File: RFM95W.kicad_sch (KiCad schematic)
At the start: 2 parts, among them U2 RFM95W-915S2

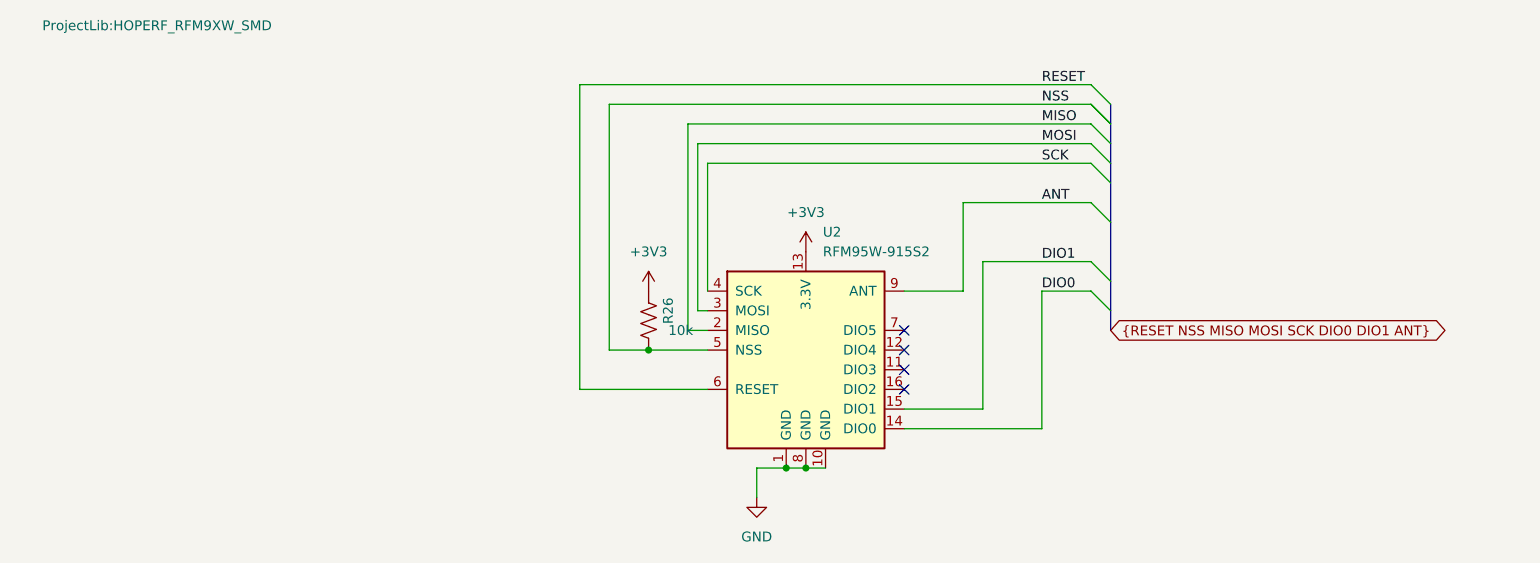
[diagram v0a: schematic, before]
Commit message: ongoing conversion to put f411 on board rather than pinsocket.
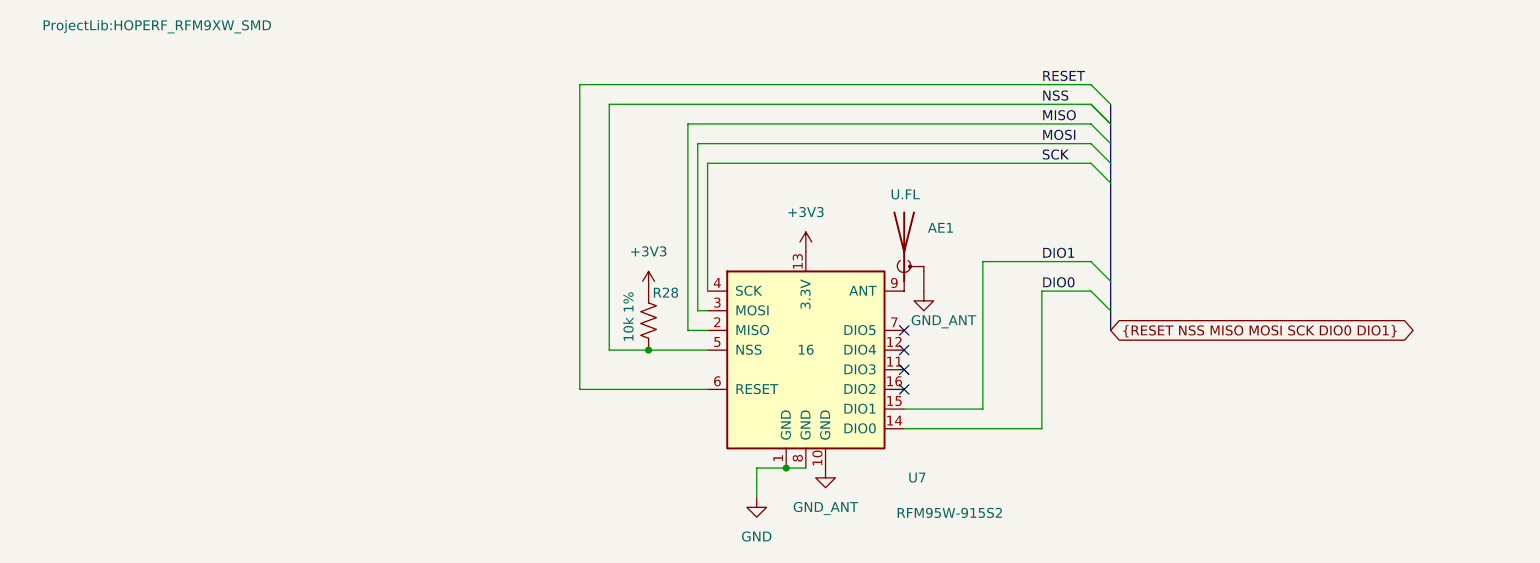
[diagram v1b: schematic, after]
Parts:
- removed R26: 10k, ProjectLib:R_0603_1608Metric, symbol ProjectLib:R_US
- added AE1: U.FL, ProjectLib:U.FL_Molex_MCRF_73412-0110_Vertical, symbol ProjectLib:Antenna_Shield
- added R28: 10k 1%, ProjectLib:R_0402_1005Metric, symbol ProjectLib:R_US
- U7: renamed from U2; Package (none) -> HOPERF_RFM9XW_SMD; pads (none) -> 16
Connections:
- net +3V3: now also R28.1
- net GND: no longer U7.10 (GND)
- net NSS: now also R28.2
- net ANT: no longer names the net of U7.9 (ANT)
- net ANT: now also AE1.1 (A)
- new net GND_ANT: AE1.2 (Shield), U7.10 (GND)
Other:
- title: Multiplex I2C to Screw Terminal connectors -> ADCs for 10K thermistors

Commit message: ongoing add of MCU, etc.
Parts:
- renumbered AE1 to AE?, R28 to R?, U7 to U?
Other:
- title: ADCs for 10K thermistors -> Multiplex I2C to Screw Terminal connectors
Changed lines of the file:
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@@
 	(paper "A4")
 	(title_block
-		(title "ADCs for 10K thermistors")
-		(date "2025-01-07")
-		(rev "v0.1.1")
+		(title "Multiplex I2C to Screw Terminal connectors")
+		(date "2025-09-07")
+		(rev "v0.2.0")
 	)
 	(bus_alias "SPI"
@@
 		(on_board yes)
 		(dnp no)
-		(property "Reference" "R28"
+		(property "Reference" "R?"
 			(at 95.758 77.724 0)
 			(effects
@@
 		)
 		(instances
-			(project ""
-				(path "/0c2d0c14-8850-4a30-bb78-b2f40cb442ba/2db29b35-1005-45eb-b852-0b853354466f"
-					(reference "R28")
+			(project "multiplexI2C"
+				(path "/0c2d0c14-8850-4a30-bb78-b2f40cb442ba/8bb5a1a1-4d5b-4032-b28f-cb44ec0cd683"
+					(reference "R?")
 					(unit 1)
 				)
@@
 		(dnp no)
 		(fields_autoplaced yes)
-		(property "Reference" "#PWR066"
+		(property "Reference" "#PWR0104"
 			(at 118.11 106.68 0)
 			(effects
@@
 		)
 		(instances
-			(project ""
-				(path "/0c2d0c14-8850-4a30-bb78-b2f40cb442ba/2db29b35-1005-45eb-b852-0b853354466f"
-					(reference "#PWR066")
+			(project "multiplexI2C"
+				(path "/0c2d0c14-8850-4a30-bb78-b2f40cb442ba/8bb5a1a1-4d5b-4032-b28f-cb44ec0cd683"
+					(reference "#PWR0104")
 					(unit 1)
 				)
@@
 		(on_board yes)
 		(dnp no)
-		(property "Reference" "#PWR065"
+		(property "Reference" "#PWR0105"
 			(at 130.81 83.82 0)
 			(effects
@@
 		)
 		(instances
-			(project ""
-				(path "/0c2d0c14-8850-4a30-bb78-b2f40cb442ba/2db29b35-1005-45eb-b852-0b853354466f"
-					(reference "#PWR065")
+			(project "multiplexI2C"
+				(path "/0c2d0c14-8850-4a30-bb78-b2f40cb442ba/8bb5a1a1-4d5b-4032-b28f-cb44ec0cd683"
+					(reference "#PWR0105")
 					(unit 1)
 				)
@@
 		)
 		(instances
-			(project "SensorProject_t16-pcb"
-				(path "/0c2d0c14-8850-4a30-bb78-b2f40cb442ba/2db29b35-1005-45eb-b852-0b853354466f"
+			(project "multiplexI2C"
+				(path "/0c2d0c14-8850-4a30-bb78-b2f40cb442ba/8bb5a1a1-4d5b-4032-b28f-cb44ec0cd683"
 					(reference "#PWR0102")
 					(unit 1)
@@
 		(dnp no)
 		(fields_autoplaced yes)
-		(property "Reference" "#PWR0103"
+		(property "Reference" "#PWR0101"
 			(at 109.22 110.49 0)
 			(effects
@@
 		)
 		(instances
-			(project "SensorProject_t16-pcb"
-				(path "/0c2d0c14-8850-4a30-bb78-b2f40cb442ba/2db29b35-1005-45eb-b852-0b853354466f"
-					(reference "#PWR0103")
+			(project "multiplexI2C"
+				(path "/0c2d0c14-8850-4a30-bb78-b2f40cb442ba/8bb5a1a1-4d5b-4032-b28f-cb44ec0cd683"
+					(reference "#PWR0101")
 					(unit 1)
 				)
@@
 		(dnp no)
 		(fields_autoplaced yes)
-		(property "Reference" "#PWR0101"
+		(property "Reference" "#PWR0103"
 			(at 115.57 76.2 0)
 			(effects
@@
 		)
 		(instances
-			(project "SensorProject_t16-pcb"
-				(path "/0c2d0c14-8850-4a30-bb78-b2f40cb442ba/2db29b35-1005-45eb-b852-0b853354466f"
-					(reference "#PWR0101")
+			(project "multiplexI2C"
+				(path "/0c2d0c14-8850-4a30-bb78-b2f40cb442ba/8bb5a1a1-4d5b-4032-b28f-cb44ec0cd683"
+					(reference "#PWR0103")
 					(unit 1)
 				)
@@
 		(on_board yes)
 		(dnp no)
-		(property "Reference" "U7"
+		(property "Reference" "U?"
 			(at 128.778 101.6 0)
 			(effects
@@
 		)
 		(instances
-			(project "SensorProject_t16-pcb"
-				(path "/0c2d0c14-8850-4a30-bb78-b2f40cb442ba/2db29b35-1005-45eb-b852-0b853354466f"
-					(reference "U7")
+			(project "multiplexI2C"
+				(path "/0c2d0c14-8850-4a30-bb78-b2f40cb442ba/8bb5a1a1-4d5b-4032-b28f-cb44ec0cd683"
+					(reference "U?")
 					(unit 1)
 				)
@@
 		(on_board yes)
 		(dnp no)
-		(property "Reference" "AE1"
+		(property "Reference" "AE?"
 			(at 131.318 69.342 0)
 			(effects
@@
 		)
 		(instances
-			(project ""
-				(path "/0c2d0c14-8850-4a30-bb78-b2f40cb442ba/2db29b35-1005-45eb-b852-0b853354466f"
-					(reference "AE1")
+			(project "multiplexI2C"
+				(path "/0c2d0c14-8850-4a30-bb78-b2f40cb442ba/8bb5a1a1-4d5b-4032-b28f-cb44ec0cd683"
+					(reference "AE?")
 					(unit 1)
 				)

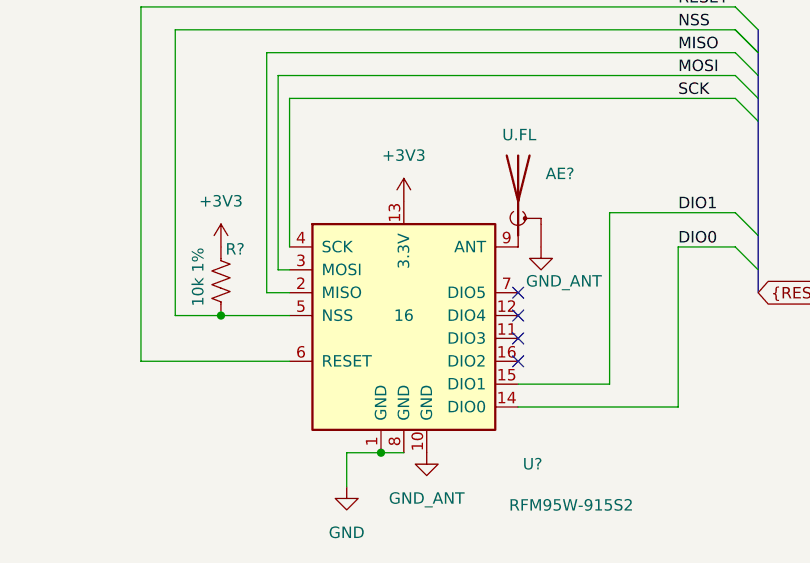
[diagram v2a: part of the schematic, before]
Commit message: symbols an footprints added for f411 change. ERC passes.
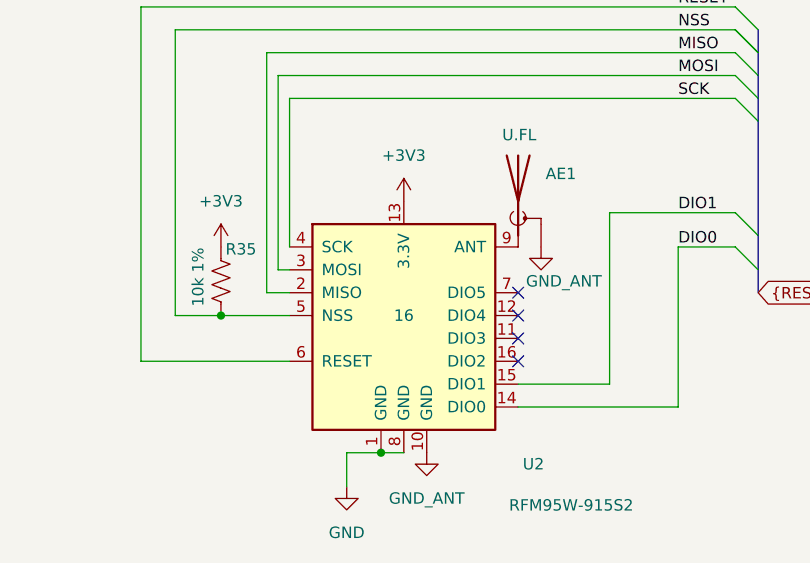
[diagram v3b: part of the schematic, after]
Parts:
- R35: renamed from R?; footprint ProjectLib:R_0402_1005Metric -> ProjectLib:R_0603_1608Metric
- gave numbers to parts that had none: 2
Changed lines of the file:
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@@
 		(on_board yes)
 		(dnp no)
-		(property "Reference" "R?"
+		(property "Reference" "R35"
 			(at 95.758 77.724 0)
 			(effects
@@
 			)
 		)
-		(property "Footprint" "ProjectLib:R_0402_1005Metric"
+		(property "Footprint" "ProjectLib:R_0603_1608Metric"
 			(at 96.266 81.534 90)
 			(effects
@@
 			)
 		)
-		(property "Datasheet" ""
+		(property "Datasheet" "~"
 			(at 95.25 81.28 0)
 			(effects
@@
 			(project "multiplexI2C"
 				(path "/0c2d0c14-8850-4a30-bb78-b2f40cb442ba/8bb5a1a1-4d5b-4032-b28f-cb44ec0cd683"
-					(reference "R?")
+					(reference "R35")
 					(unit 1)
 				)
@@
 		(on_board yes)
 		(dnp no)
-		(property "Reference" "U?"
+		(property "Reference" "U2"
 			(at 128.778 101.6 0)
 			(effects
@@
 			)
 		)
-		(property "Datasheet" "https://cdn.sparkfun.com/assets/learn_tutorials/8/0/4/RFM95_96_97_98W.pdf"
+		(property "Datasheet" "https://www.hoperf.com/modules/lora/RFM95W.html"
 			(at 31.75 43.18 0)
 			(effects
@@
 			)
 		)
-		(property "Description" "LoRa module, SPI, 915 MHz,  SMD-16"
+		(property "Description" "LoRa module, SPI, 915MHz, spreading factor 6 to12, bandwidth 125 to 500kHz, -111 to -136 dBm, SMD-16"
 			(at 115.57 85.09 0)
 			(effects
@@
 			(project "multiplexI2C"
 				(path "/0c2d0c14-8850-4a30-bb78-b2f40cb442ba/8bb5a1a1-4d5b-4032-b28f-cb44ec0cd683"
-					(reference "U?")
+					(reference "U2")
 					(unit 1)
 				)
@@
 		(on_board yes)
 		(dnp no)
-		(property "Reference" "AE?"
+		(property "Reference" "AE1"
 			(at 131.318 69.342 0)
 			(effects
@@
 			)
 		)
-		(property "Datasheet" "https://www.hirose.com/en/product/document?clcode=CL0331-0472-2-60&productname=U.FL-R-SMT-1(60)&series=U.FL&documenttype=Catalog&lang=en&documentid=ed_U.FL_CAT"
+		(property "Datasheet" "~"
 			(at 128.27 69.85 0)
 			(effects
@@
 			)
 		)
-		(property "Description" "Antenna connector with shielding"
+		(property "Description" "Antenna with extra pin for shielding"
 			(at 128.27 72.39 0)
 			(effects
@@
 			(project "multiplexI2C"
 				(path "/0c2d0c14-8850-4a30-bb78-b2f40cb442ba/8bb5a1a1-4d5b-4032-b28f-cb44ec0cd683"
-					(reference "AE?")
+					(reference "AE1")
 					(unit 1)
 				)
